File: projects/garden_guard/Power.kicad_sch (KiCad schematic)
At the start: 0 parts

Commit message: - Add PoE 12V power module - Add 12V->5V buck - Add automatic power source selection between PoE 5V and USB 5V
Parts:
- added BR1, BR2: CDBHD2100-G, Custom_PoE:CDBHD2100-G, symbol Custom_PoE:CDBHD2100-G
- added C12, C9: 10uF, Custom_PoE:CL31A106MAHNNNE, symbol Device:C_Small
- added C13: 2.2uF, symbol Device:C_Small
- added C18, C20: 4.7nF, symbol Device:C_Small
- added C2, C8: 1000uF, symbol Device:C_Polarized_Small_US
- added C21, C23, C25: 0.1uF, symbol Device:C_Small
- added C22, C24: 4.7uF, symbol Device:C_Small
- added C26, C27, C28, C29: 22uF, symbol Device:C_Small
- added C3, C7: 100n, Capacitor_SMD:C_0402_1005Metric, symbol Device:C
- added C30: 100nF, symbol Device:C_Small
- added D4: SMAJ58A, Diode_SMD:D_SMA, symbol Diode:SMAJ58A
- added FB1, FB2, FB3, FB4, FB5, FB6: 1kOhm, symbol Device:FerriteBead_Small
- added IC1: ACPL-227-50CE, Custom_PoE:SOIC127P700X220-8N, symbol Custom_PoE:ACPL-227-50CE
- added J10: USB_C_Receptacle_USB2.0, Connector_USB:USB_C_Receptacle_GCT_USB4105-xx-A_16P_TopMnt_Horizontal, symbol Connector:USB_C_Receptacle_USB2.0_16P
- added L2: 0.47uH, symbol Device:L_Small
- added R12, R9: 10k, symbol Device:R_Small_US
- added R18: 22.1k, symbol Device:R_Small_US
- added R19: 2.2K 1%, Resistor_SMD:R_0402_1005Metric, symbol Device:R
- added TP6: 12V_PGOOD_TP, symbol Connector:TestPoint
- added U5: MAX20408AFOF, Custom_DCDC:MAX20408AFOF, symbol Custom_DCDC:MAX20408AFOF
- added U6: TPS2121RUXR, Custom_DCDC:TPS2121RUXR, symbol Custom_DCDC:TPS2121RUXR
- added U9: Ag5810, Custom_PoE:Ag5810, symbol Custom_PoE:Ag5810
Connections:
- new net: BR1.4 (-), BR2.4 (-), D4.2 (A2), FB4.1
- new net: FB4.2, FB5.1
- new net: BR1.3 (+), BR2.3 (+), D4.1 (A1), FB1.1
- new net: FB1.2, FB2.1
- new net: FB2.2, FB3.1
- new net: IC1.1 (ANODE_1), R9.2
- new net: IC1.2 (CATHODE_1), U9.3 (TYP2-DET)
- new net: IC1.3 (ANODE_2), R12.2
- new net: IC1.4 (CATHODE_2), U9.4 (TYP4-DET)
- new net: C20.1, FB6.2, U9.2 (VIN-)
- new net: C18.1, FB3.2, U9.1 (VIN+)
- new net: C30.1, U6.11 (SS)
- new net: FB5.2, FB6.1
- new net: C13.1, U5.11 (BIAS), U5.12 (FB), U5.16 (SYNC)
- new net: TP6.1, U5.15 (PGOOD)
- new net: C25.2, U5.2 (BST)
- new net: C25.1, L2.2, U5.6 (LX)
- new net: R18.1, U6.10 (ILIM)
- new net +12v: C12.1, C2.1, C21.1, C22.1, C23.1, C24.1, C8.1, C9.1, R12.1, R9.1, U5.1 (EN), U5.3 (SUP), U5.9 (SUP), U9.10 (VOUT2), U9.7 (VOUT1), U9.8 (VOUT1)
- new net +5v: C3.1, C7.1, U6.1 (OUT), U6.8 (OUT)
- new net +5v_poe: C26.1, C27.1, C28.1, C29.1, L2.1, U5.13 (OUT), U6.7 (IN1)
- new net +5v_usb: J10.A4 (VBUS), J10.A9 (VBUS), J10.B4 (VBUS), J10.B9 (VBUS), R19.1, U6.2 (IN2)
- new net CC1: J10.A5 (CC1)
- new net CC2: J10.B5 (CC2)
- new net GND: C12.2, C13.2, C18.2, C2.2, C20.2, C21.2, C22.2, C23.2, C24.2, C26.2, C27.2, C28.2, C29.2, C3.2, C30.2, C7.2, C8.2, C9.2, IC1.5 (EMITTER_1), IC1.7 (EMITTER_2), J10.A1 (GND), J10.A12 (GND), J10.B1 (GND), J10.B12 (GND), J10.S1 (SHIELD), R18.2, R19.2, U5.10 (GND), U5.4 (PGND), U5.5 (PGND), U5.7 (PGND), U5.8 (PGND), U6.12 (GND), U6.3 (CP2), U6.4 (OV2), U6.5 (OV1), U6.6 (PR1), U9.11 (0V2), U9.12 (0V2), U9.9 (0v1)
- new net PWR_SRC_SEL: U6.9 (ST)
- new net PoE++_actv: IC1.6 (COLLECTOR_1)
- new net PoE+_actv: IC1.8 (COLLECTOR_2)
- new net TR0_TAP: BR1.1 (~_1)
- new net TR1_TAP: BR1.2 (~_2)
- new net TR2_TAP: BR2.1 (~_1)
- new net TR3_TAP: BR2.2 (~_2)
- new net USB2_N: J10.A7 (D-), J10.B7 (D-)
- new net USB2_P: J10.A6 (D+), J10.B6 (D+)
- no-connect marks 0 -> 7
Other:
- note added: "12v to 5V Buck"
- note added: "5V Power Source Select"
- note added: "Discharge Resistor Needed by some USB-C PSUs"
- note added: "Global +12v Source"
- note added: "Global +5v Source"
- note added: "Global Ground Source"
- note added: "PoE DC-DC"
- note added: "PoE Status Isolator"
- note added: "USB-C Power Connector"

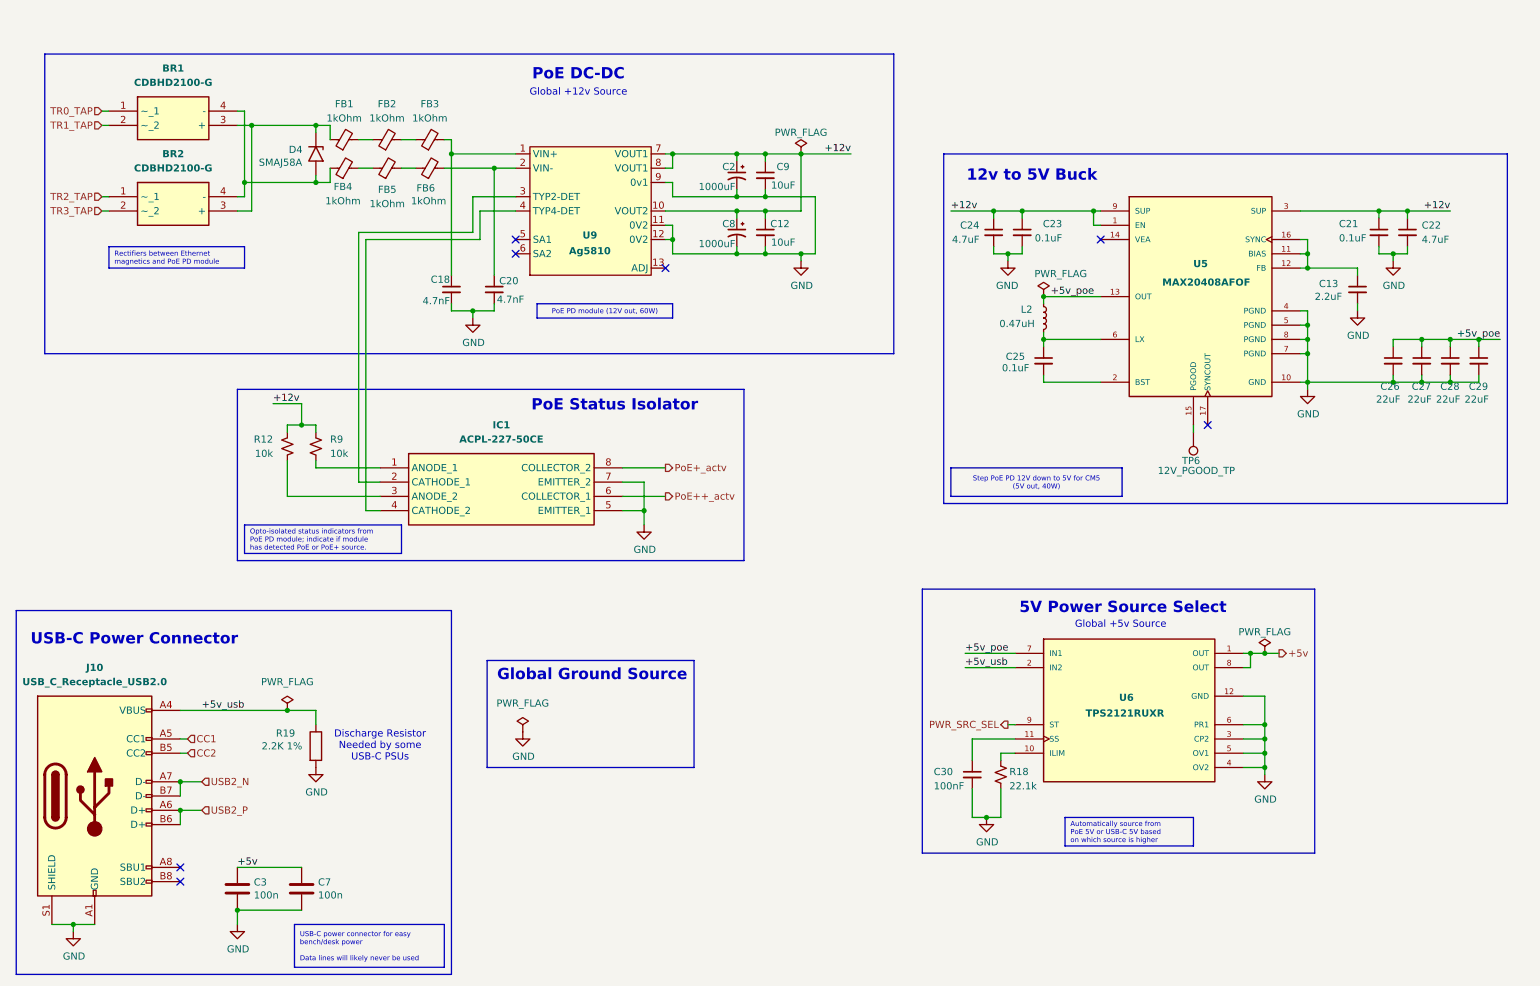
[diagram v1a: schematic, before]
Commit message: - Add 12V and 5V power sensing - Add solenoid and IR illum outputs, power expansion, an peripheral comms - General clean-up - Remove .bak files mistakenly added in previous commits - Add *.bak to .gitignore
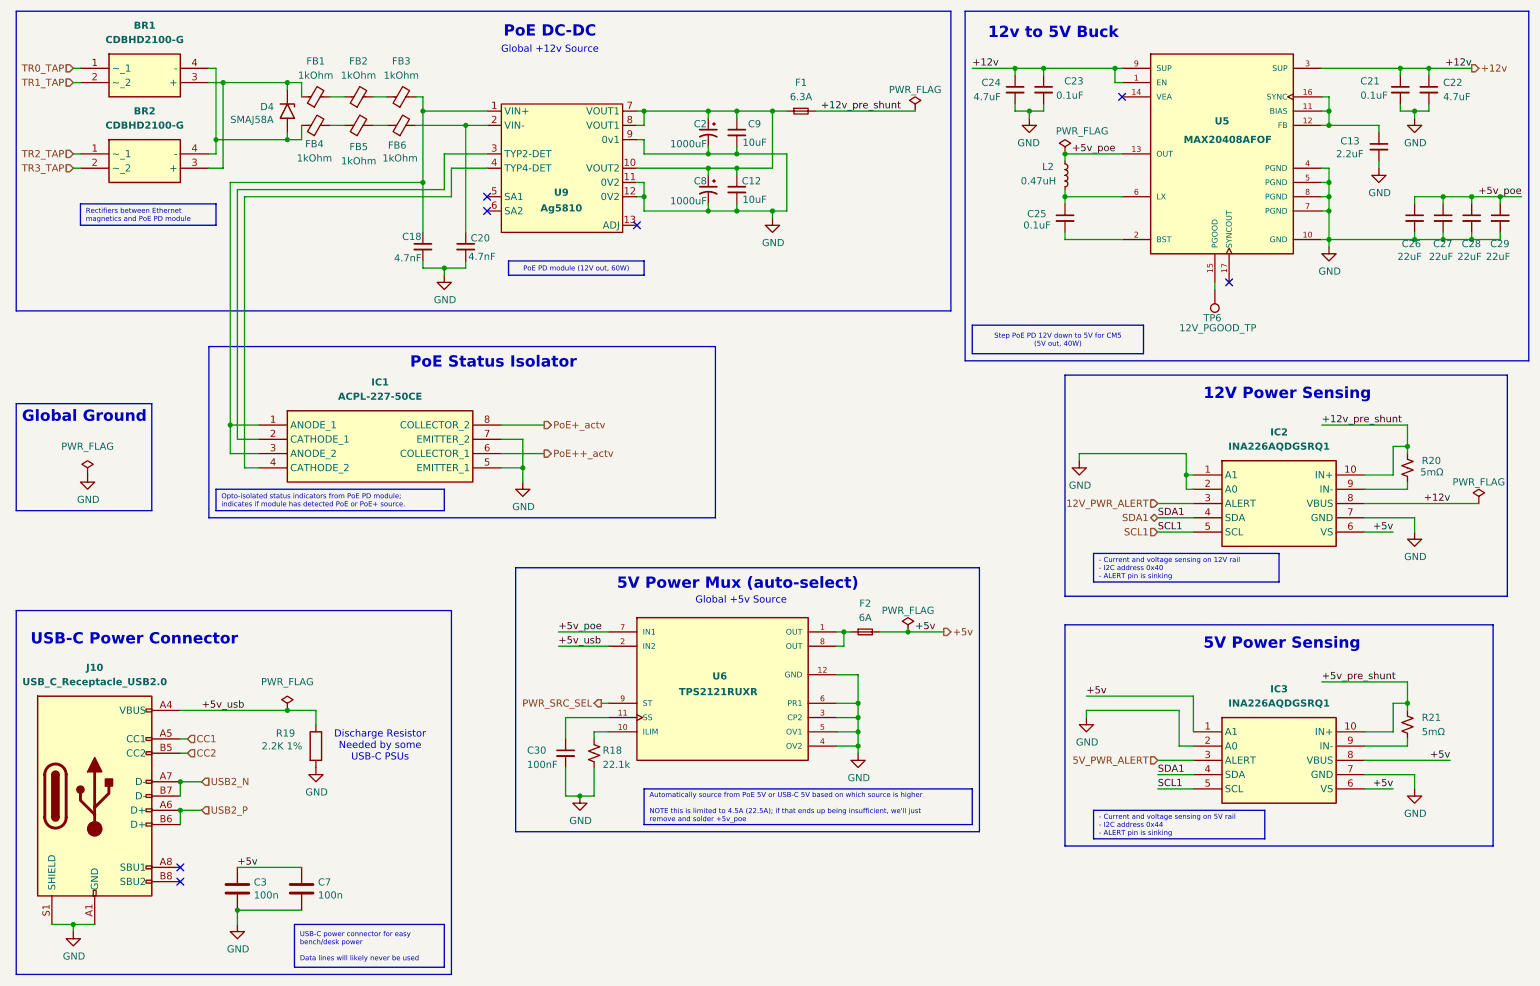
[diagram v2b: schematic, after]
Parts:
- removed R12, R9: 10k, symbol Device:R_Small_US
- added F1: 6.3A, Fuse:Fuse_1206_3216Metric, symbol Device:Fuse_Small
- added F2: 6A, Fuse:Fuse_0603_1608Metric, symbol Device:Fuse_Small
- added IC2, IC3: INA226AQDGSRQ1, Custom_Sensor:INA226AQDGSRQ1, symbol Custom_Sensor:INA226AQDGSRQ1
- added R20, R21: 5mΩ, symbol Device:R_Small_US
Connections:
- net +12v: now also IC2.8 (VBUS); no longer C12.1, C2.1, C8.1, C9.1, U9.10 (VOUT2), U9.7 (VOUT1), U9.8 (VOUT1)
- net +5v: now also F2.2, IC2.6 (VS), IC3.1 (A1), IC3.6 (VS), IC3.8 (VBUS); no longer U6.1 (OUT), U6.8 (OUT)
- net GND: now also IC2.1 (A1), IC2.2 (A0), IC2.7 (GND), IC3.2 (A0), IC3.7 (GND)
- net at IC1.1 (ANODE_1): now also C18.1, FB3.2, IC1.3 (ANODE_2), U9.1 (VIN+)
- new net: C12.1, C2.1, C8.1, C9.1, F1.1, U9.10 (VOUT2), U9.7 (VOUT1), U9.8 (VOUT1)
- new net: IC2.9 (IN-), R20.2
- new net: IC3.9 (IN-), R21.2
- new net: F2.1, U6.1 (OUT), U6.8 (OUT)
- new net +12v_pre_shunt: F1.2, IC2.10 (IN+), R20.1
- new net +5v_pre_shunt: IC3.10 (IN+), R21.1
- new net 12V_PWR_ALERT: IC2.3 (ALERT)
- new net 5V_PWR_ALERT: IC3.3 (ALERT)
- new net SCL1: IC2.5 (SCL), IC3.5 (SCL)
- new net SDA1: IC2.4 (SDA), IC3.4 (SDA)
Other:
- note added: "12V Power Sensing"
- note added: "5V Power Mux (auto-select)"
- note added: "5V Power Sensing"
- note added: "Global Ground"
- note removed: "5V Power Source Select"
- note removed: "Global Ground Source"
- moved on the sheet: BR1, BR2, C12, C13, C18, C2, C20, C21, C22, C23, C24, C25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

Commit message: - Add all missing footprints - Add specific part numbers to each component in schematic
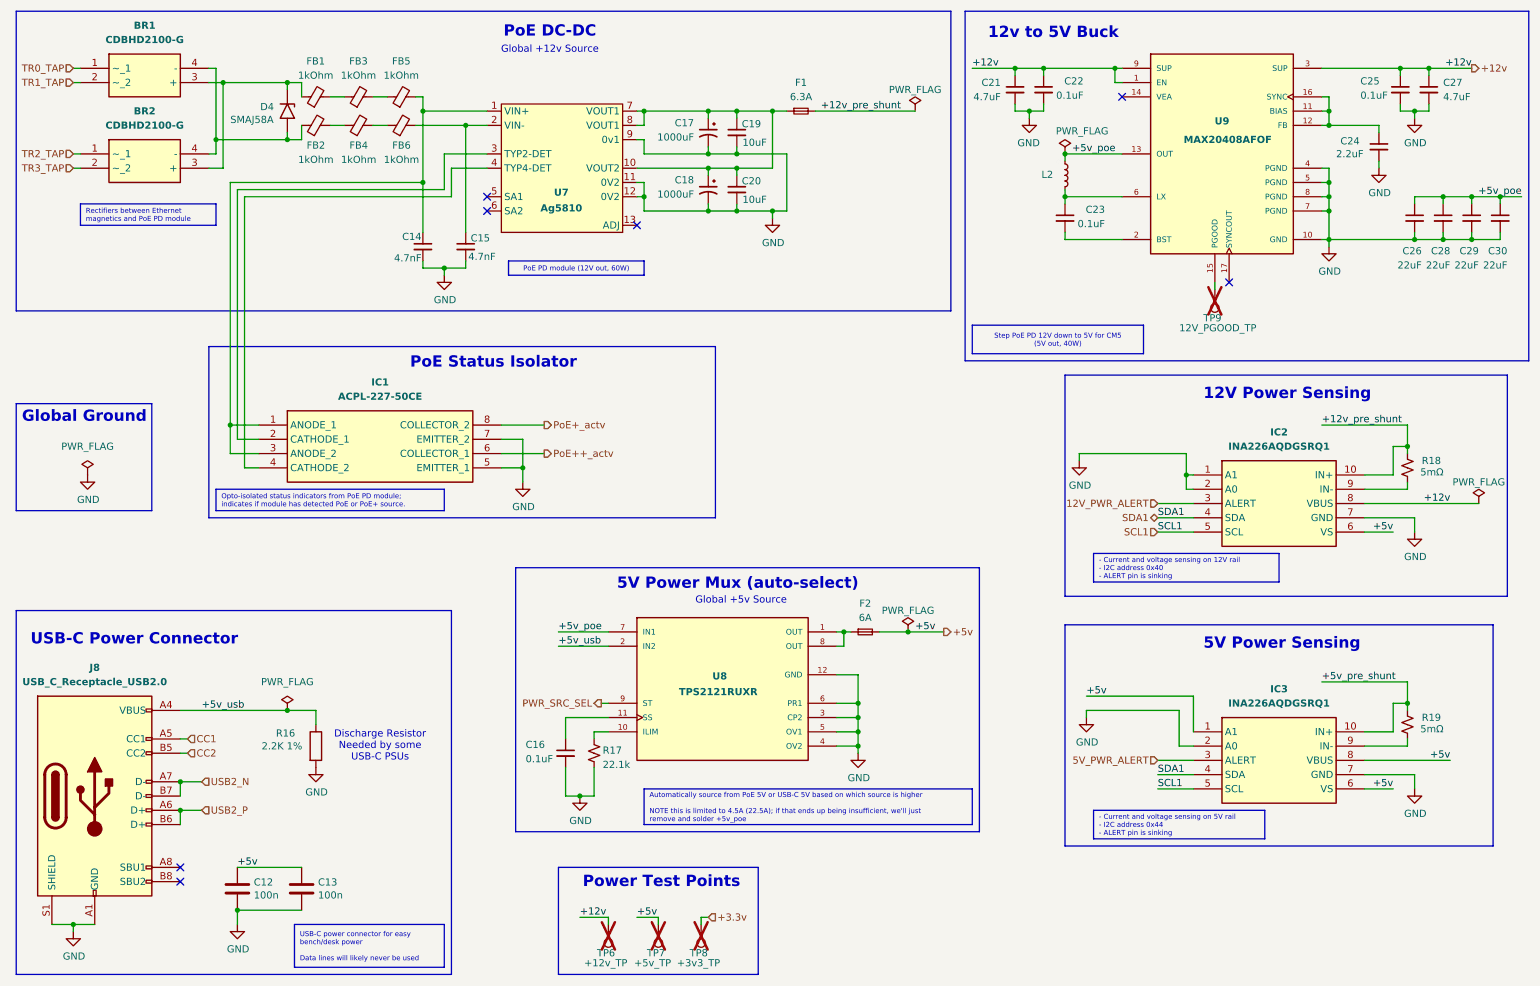
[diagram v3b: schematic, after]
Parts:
- removed C2, C8: 1000uF, symbol Device:C_Polarized_Small_US
- removed C21: 0.1uF, symbol Device:C_Small
- removed C22: 4.7uF, symbol Device:C_Small
- removed L2: 0.47uH, symbol Device:L_Small
- removed R21: 5mΩ, symbol Device:R_Small_US
- added C16, C23: 0.1uF, Resistor_SMD:R_0603_1608Metric, symbol Device:C_Small
- added C17, C18: 1000uF, Custom_PoE:EEE-FT1E102UP, symbol Custom_PoE:EEE-FT1E102UP
- added L2: ETQ-P4M2R2KFM, Custom_DCDC:ETQ-P4M2R2KFM, symbol Custom_DCDC:ETQ-P4M2R2KFM
- added R19: 5mΩ, Resistor_SMD:R_0603_1608Metric, symbol Device:R_Small_US
- added TP6: +12v_TP, TestPoint:TestPoint_Pad_2.0x2.0mm, symbol Connector:TestPoint
- added TP7: +5v_TP, TestPoint:TestPoint_Pad_2.0x2.0mm, symbol Connector:TestPoint
- added TP8: +3v3_TP, TestPoint:TestPoint_Pad_2.0x2.0mm, symbol Connector:TestPoint
- C14: renamed from C18; footprint (none) -> Custom_PoE:C1812C472KGRACAUTO; Manufacturer KEMET -> (none); Mfr (none) -> KEMET
- C15: renamed from C20; footprint (none) -> Custom_PoE:C1812C472KGRACAUTO; Manufacturer KEMET -> (none); Mfr (none) -> KEMET
- C19: renamed from C9; Manufacturer Samsung -> (none); Mfr (none) -> Samsung
- C20: renamed from C12; Manufacturer Samsung -> (none); Mfr (none) -> Samsung
- C21: renamed from C24; footprint (none) -> Capacitor_SMD:C_0603_1608Metric; MPN (none) -> GRM188R61E475KE11D; Mfr (none) -> Murata Electronics
- C22: renamed from C23; footprint (none) -> Resistor_SMD:R_0603_1608Metric; MPN (none) -> C0603C104K3RACTU; Manufacturer (none) -> KEMET
- C24: renamed from C13; footprint (none) -> Capacitor_SMD:C_0201_0603Metric; MPN (none) -> GRM188R61E225KA12D; Mfr (none) -> Murata Electronics
- C25: footprint (none) -> Resistor_SMD:R_0603_1608Metric; MPN (none) -> C0603C104K3RACTU; Manufacturer (none) -> KEMET
- C26, C28, C29: footprint (none) -> Capacitor_SMD:C_0603_1608Metric; MPN (none) -> GRM21BR61E226ME44L; Mfr (none) -> Murata Electronics
- C27: value 22uF -> 4.7uF; footprint (none) -> Capacitor_SMD:C_0603_1608Metric; MPN (none) -> GRM188R61E475KE11D; Mfr (none) -> Murata Electronics
- C30: value 100nF -> 22uF; footprint (none) -> Capacitor_SMD:C_0603_1608Metric; MPN (none) -> GRM21BR61E226ME44L; Mfr (none) -> Murata Electronics
- D4: MPN (none) -> SMAJ58A; Mfr (none) -> Bourns Inc.
- FB1, FB2, FB3, FB4, FB5, FB6: footprint (none) -> Fuse:Fuse_1210_3225Metric; MPN (none) -> FBMH3225HM102NT; Mfr (none) -> Taiyo Yuden
- R17: renamed from R18; footprint (none) -> Resistor_SMD:R_0603_1608Metric; MPN (none) -> RC0603FR-0722K1L; Mfr (none) -> YAGEO
- R18: renamed from R20; footprint (none) -> Resistor_SMD:R_0603_1608Metric; MPN (none) -> ERJ-3LWFR005V; Mfr (none) -> Panasonic
- TP9: renamed from TP6; footprint (none) -> TestPoint:TestPoint_Pad_2.0x2.0mm; now not fitted; now left out of the parts list
- renumbered C3 to C12, C7 to C13, J10 to J8, R19 to R16, U9 to U7, U6 to U8, U5 to U9
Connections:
- net +12v: now also C25.1, C27.1, TP6.1
- net +5v: now also TP7.1
- net +5v_poe: now also C30.1, L2.1; no longer C27.1
- net +5v_pre_shunt: now also R19.1
- net GND: now also C25.2, C16.2, C17.2, C18.2
- net at BR1.4 (-), BR2.4 (-), D4.2 (A2): now also FB2.1; no longer FB4.1
- net at FB5.1: now also FB3.2; no longer FB4.2
- net at C19.1, C20.1, F1.1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: now also C17.1, C18.1
- net at FB1.2: now also FB3.1; no longer FB2.1
- net at FB2.2: now also FB4.1; no longer FB3.1
- net at C14.1, IC1.1 (ANODE_1), IC1.3 (ANODE_2)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: now also FB5.2; no longer FB3.2
- net at IC3.9 (IN-): now also R19.2
- net at U8.11 (SS): now also C16.1; no longer C30.1
- net at FB6.1: now also FB4.2; no longer FB5.2
- net at U9.2 (BST): now also C23.2; no longer C25.2
- net at U9.6 (LX): now also C23.1, L2.2; no longer C25.1
- new net +3.3v: TP8.1
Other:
- note added: "Power Test Points"
